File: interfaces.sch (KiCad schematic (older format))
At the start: 74 parts, among them J6 0878311420, J7 61300611121, U1 MTFC16GAPALNA-AIT, U14 XC7A100T-FGG484, U17 USB3300-EZK-TR, U18 USB3300-EZK-TR, U6 NVT2008DQ,115, Y1 TSX-3225, Y3 TSX-3225

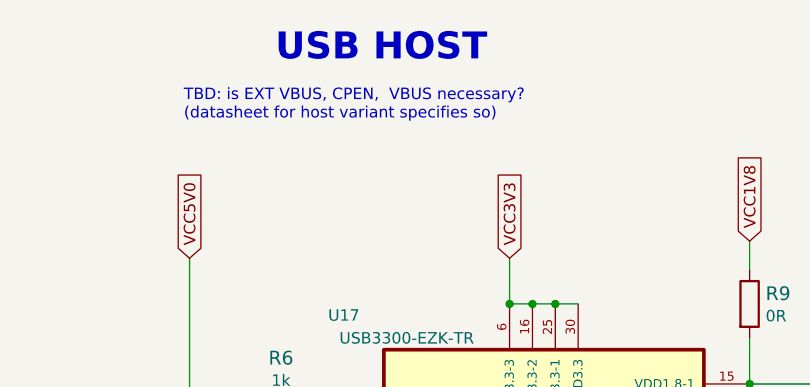
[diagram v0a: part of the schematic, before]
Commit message: Update schematic notes, update SPI0 connection
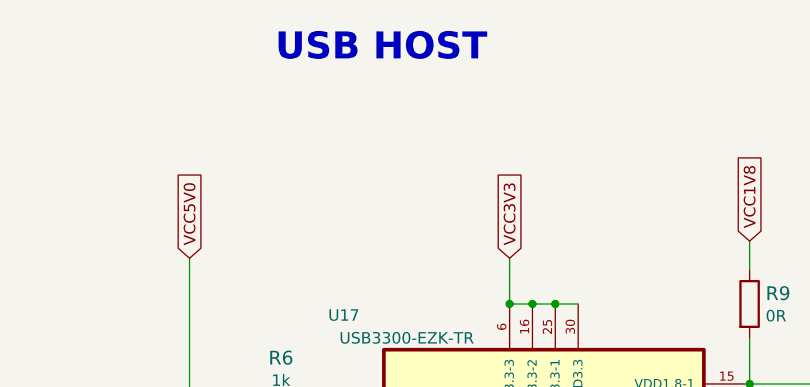
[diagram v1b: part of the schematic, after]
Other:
- note removed: "TBD: is EXT VBUS, CPEN, VBUS necessary?\n(datasheet for host variant specifies so)"
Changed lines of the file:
@@
 NoConn ~ 11400 6900
 NoConn ~ 11300 3400
-Text Notes 10625 1150 0    50   ~ 0
-TBD: is EXT VBUS, CPEN,  VBUS necessary?\n(datasheet for host variant specifies so)
 $Comp
 L artix-dc-scm:R_1M5_0402 R4

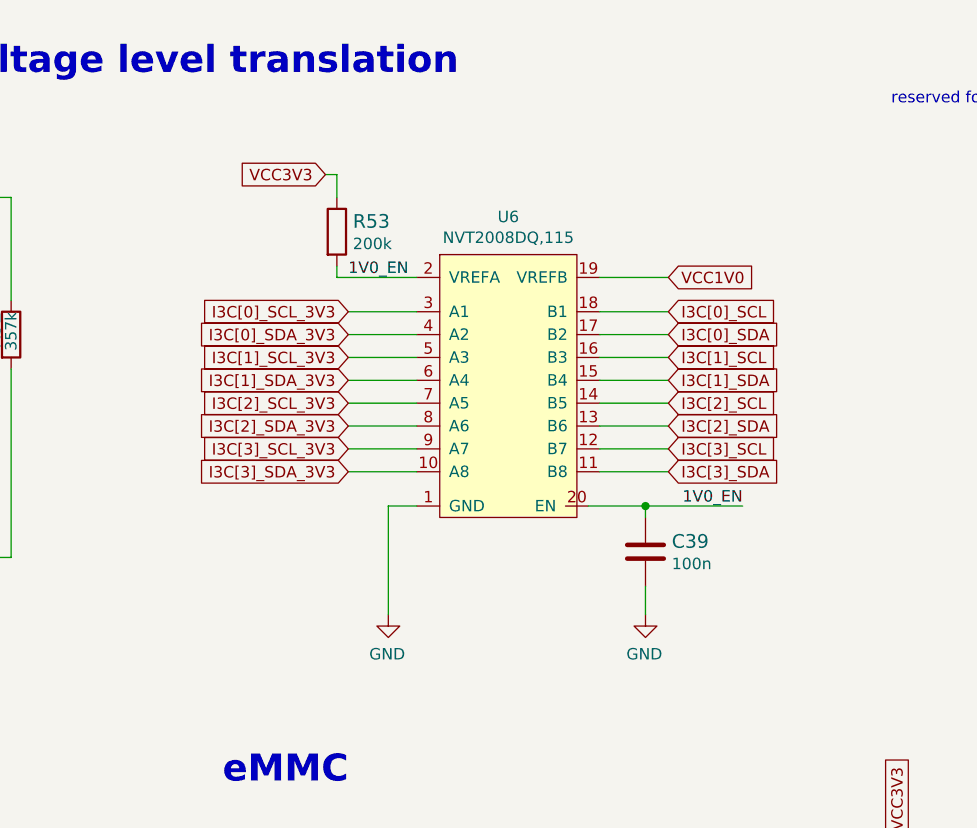
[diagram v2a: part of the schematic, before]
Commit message: Fix 1v0 translator
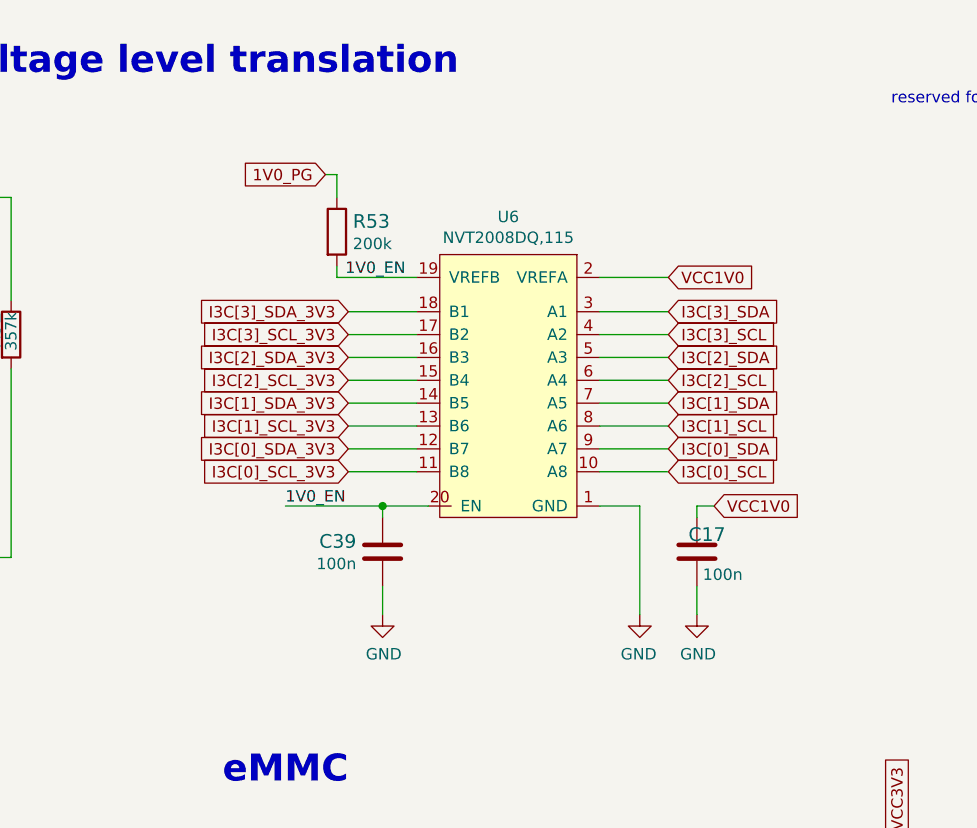
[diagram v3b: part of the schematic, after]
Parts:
- added C17: C_100n_0402, artix-dc-scm-footprints:0402-cap, symbol artix-dc-scm:C_100n_0402-artix-dc-scm
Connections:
- net 1V0_EN: now also U6.19 (VREFB); no longer U6.2 (VREFA)
- net GND: now also C17.1
- net I3C[0]_SCL: now also U6.10 (A8); no longer U6.18 (B1)
- net I3C[0]_SCL_3V3: now also U6.11 (B8); no longer U6.3 (A1)
- net I3C[0]_SDA: now also U6.9 (A7); no longer U6.17 (B2)
- net I3C[0]_SDA_3V3: now also U6.12 (B7); no longer U6.4 (A2)
- net I3C[1]_SCL: now also U6.8 (A6); no longer U6.16 (B3)
- net I3C[1]_SCL_3V3: now also U6.13 (B6); no longer U6.5 (A3)
- net I3C[1]_SDA: now also U6.7 (A5); no longer U6.15 (B4)
- net I3C[1]_SDA_3V3: now also U6.14 (B5); no longer U6.6 (A4)
- net I3C[2]_SCL: now also U6.6 (A4); no longer U6.14 (B5)
- net I3C[2]_SCL_3V3: now also U6.15 (B4); no longer U6.7 (A5)
- net I3C[2]_SDA: now also U6.5 (A3); no longer U6.13 (B6)
- net I3C[2]_SDA_3V3: now also U6.16 (B3); no longer U6.8 (A6)
- net I3C[3]_SCL: now also U6.4 (A2); no longer U6.12 (B7)
- net I3C[3]_SCL_3V3: now also U6.17 (B2); no longer U6.9 (A7)
- net I3C[3]_SDA: now also U6.3 (A1); no longer U6.11 (B8)
- net I3C[3]_SDA_3V3: now also U6.18 (B1); no longer U6.10 (A8)
- net VCC1V0: now also U6.2 (VREFA), C17.2; no longer U6.19 (VREFB)
- net VCC3V3: no longer R53.1
- new net 1V0_PG: R53.1
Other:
- moved on the sheet: C39
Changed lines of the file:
@@
 JTAG
-$Comp
-L artix-dc-scm:NVT2008DQ,115-artix-dc-scm U6
-U 1 1 628E0C73
-P 5000 6025
-F 0 "U6" H 5000 6540 50  0000 C CNN
-F 1 "NVT2008DQ,115" H 5000 6449 50  0000 C CNN
-F 2 "artix-dc-scm-footprints:QFN50P250X450X100-21N" H 5700 6775 50  0001 C CNN
-F 3 "" H 5650 6775 50  0001 C CNN
-F 4 "NVT2008BQ,115" H 5300 6875 50  0001 C CNN "MPN"
-F 5 "NXP Semiconductors" H 5400 6975 50  0001 C CNN "Manufacturer"
-	1    5000 6025
-	1    0    0    -1
-$EndComp
-Text GLabel 4300 6025 0    50   Input ~ 0
-I3C[0]_SDA_3V3
-Text GLabel 4300 6225 0    50   Input ~ 0
-I3C[1]_SDA_3V3
-Text GLabel 4300 6125 0    50   Input ~ 0
-I3C[1]_SCL_3V3
-Text GLabel 4300 6425 0    50   Input ~ 0
-I3C[2]_SDA_3V3
-Text GLabel 4300 6325 0    50   Input ~ 0
-I3C[2]_SCL_3V3
-Text GLabel 4300 6625 0    50   Input ~ 0
-I3C[3]_SDA_3V3
-Text GLabel 4300 6525 0    50   Input ~ 0
-I3C[3]_SCL_3V3
-Text GLabel 4300 5925 0    50   Input ~ 0
-I3C[0]_SCL_3V3
-Text GLabel 5700 5775 2    50   Input ~ 0
-VCC1V0
-$Comp
-L artix-dc-scm:GND-artix-dc-scm #PWR032
-U 1 1 628E4783
-P 4475 7250
-F 0 "#PWR032" H 4475 7000 50  0001 C CNN
-F 1 "GND" H 4480 7077 50  0000 C CNN
-F 2 "" H 4475 7250 50  0001 C CNN
-F 3 "" H 4475 7250 50  0001 C CNN
-	1    4475 7250
-	-1   0    0    -1
-$EndComp
-Wire Wire Line
-	4600 6775 4475 6775
-Wire Wire Line
-	4475 6775 4475 7250
-Wire Wire Line
-	4600 5925 4300 5925
-Wire Wire Line
-	4600 6025 4300 6025
-Wire Wire Line
-	4600 6125 4300 6125
-Wire Wire Line
-	4600 6225 4300 6225
-Wire Wire Line
-	4600 6325 4300 6325
-Wire Wire Line
-	4600 6425 4300 6425
-Wire Wire Line
-	4600 6525 4300 6525
-Wire Wire Line
-	4600 6625 4300 6625
-Wire Wire Line
-	5400 5925 5700 5925
-Wire Wire Line
-	5400 6025 5700 6025
-Wire Wire Line
-	5400 6125 5700 6125
-Wire Wire Line
-	5400 6225 5700 6225
-Wire Wire Line
-	5400 6325 5700 6325
-Wire Wire Line
-	5400 6425 5700 6425
-Wire Wire Line
-	5400 6525 5700 6525
-Wire Wire Line
-	5400 6625 5700 6625
-Text GLabel 4200 5325 0    50   Input ~ 0
-VCC3V3
-Wire Wire Line
-	4600 5775 4250 5775
-Wire Wire Line
-	5700 5775 5400 5775
-Wire Wire Line
-	6025 6775 5600 6775
-Text Label 6025 6775 2    50   ~ 0
-1V0_EN
 $Comp
 L artix-dc-scm:R_357k_0402-artix-dc-scm R46
@@
 Wire Wire Line
 	2725 5425 2825 5425
-$Comp
-L artix-dc-scm:R_200k_0402-artix-dc-scm R53
-U 1 1 61B2DA1A
-P 4250 5575
-F 0 "R53" V 4205 5645 60  0000 L CNN
-F 1 "R_200k_0402" H 4250 5425 60  0001 C CNN
-F 2 "artix-dc-scm-footprints:0402-res" H 4450 5775 60  0001 L CNN
-F 3 "" H 4250 5575 50  0001 C CNN
-F 4 "YAGEO_(PHYCOMP)" H 4450 5975 60  0001 L CNN "Manufacturer"
-F 5 "RC0402FR-07200KL" H 4450 5875 60  0001 L CNN "MPN"
-F 6 "200k" V 4303 5645 50  0000 L CNN "Val"
-	1    4250 5575
-	0    1    1    0
-$EndComp
-Wire Wire Line
-	4250 5775 4250 5725
-Wire Wire Line
-	4250 5425 4250 5325
-Wire Wire Line
-	4200 5325 4250 5325
-Text Label 4300 5775 0    50   ~ 0
-1V0_EN
-$Comp
-L artix-dc-scm:C_100n_0402-artix-dc-scm C39
-U 1 1 61B2DA1B
-P 5600 6975
-F 0 "C39" H 5485 6930 60  0000 R CNN
-F 1 "C_100n_0402" H 5600 6825 60  0001 C CNN
-F 2 "artix-dc-scm-footprints:0402-cap" H 5800 7175 60  0001 L CNN
-F 3 "" H 5600 6975 50  0001 C CNN
-F 4 "Walsin" H 5800 7375 60  0001 L CNN "Manufacturer"
-F 5 "0402X104K6R3CT" H 5800 7275 60  0001 L CNN "MPN"
-F 6 "100n" H 5485 7028 50  0000 R CNN "Val"
-	1    5600 6975
-	-1   0    0    1
-$EndComp
-Wire Wire Line
-	5600 6775 5600 6825
-Connection ~ 5600 6775
-Wire Wire Line
-	5600 6775 5350 6775
-$Comp
-L artix-dc-scm:GND-artix-dc-scm #PWR034
-U 1 1 61B2DA1C
-P 5600 7250
-F 0 "#PWR034" H 5600 7000 50  0001 C CNN
-F 1 "GND" H 5605 7077 50  0000 C CNN
-F 2 "" H 5600 7250 50  0001 C CNN
-F 3 "" H 5600 7250 50  0001 C CNN
-	1    5600 7250
-	-1   0    0    -1
-$EndComp
-Wire Wire Line
-	5600 7125 5600 7250
 Text Notes 2200 4900 0    118  ~ 24
 I3C voltage level translation
@@
 Wire Wire Line
 	2125 2850 2125 2725
-Text GLabel 5700 5925 2    50   Input ~ 0
-I3C[0]_SCL
-Text GLabel 5700 6025 2    50   Input ~ 0
-I3C[0]_SDA
-Text GLabel 5700 6125 2    50   Input ~ 0
-I3C[1]_SCL
-Text GLabel 5700 6225 2    50   Input ~ 0
-I3C[1]_SDA
-Text GLabel 5700 6325 2    50   Input ~ 0
-I3C[2]_SCL
-Text GLabel 5700 6425 2    50   Input ~ 0
-I3C[2]_SDA
-Text GLabel 5700 6525 2    50   Input ~ 0
-I3C[3]_SCL
-Text GLabel 5700 6625 2    50   Input ~ 0
-I3C[3]_SDA
 $Comp
 L artix-dc-scm:C_100n_0402-artix-dc-scm C189
@@
 Text Notes 4650 1350 0    50   ~ 0
 TODO: The PCIe x1 connection must be confirmed by synthesis
+$Comp
+L artix-dc-scm:NVT2008DQ,115-artix-dc-scm U6
+U 1 1 628E0C73
+P 5000 6025
+F 0 "U6" H 5000 6540 50  0000 C CNN
+F 1 "NVT2008DQ,115" H 5000 6449 50  0000 C CNN
+F 2 "artix-dc-scm-footprints:QFN50P250X450X100-21N" H 5700 6775 50  0001 C CNN
+F 3 "" H 5650 6775 50  0001 C CNN
+F 4 "NVT2008BQ,115" H 5300 6875 50  0001 C CNN "MPN"
+F 5 "NXP Semiconductors" H 5400 6975 50  0001 C CNN "Manufacturer"
+	1    5000 6025
+	-1   0    0    -1
+$EndComp
+Wire Wire Line
+	4450 7125 4450 7250
+$Comp
+L artix-dc-scm:GND-artix-dc-scm #PWR034
+U 1 1 61B2DA1C
+P 4450 7250
+F 0 "#PWR034" H 4450 7000 50  0001 C CNN
+F 1 "GND" H 4455 7077 50  0000 C CNN
+F 2 "" H 4450 7250 50  0001 C CNN
+F 3 "" H 4450 7250 50  0001 C CNN
+	1    4450 7250
+	1    0    0    -1
+$EndComp
+Wire Wire Line
+	4450 6775 4650 6775
+Connection ~ 4450 6775
+Wire Wire Line
+	4450 6775 4450 6825
+$Comp
+L artix-dc-scm:C_100n_0402-artix-dc-scm C39
+U 1 1 61B2DA1B
+P 4450 6975
+F 0 "C39" H 4335 6930 60  0000 R CNN
+F 1 "C_100n_0402" H 4450 6825 60  0001 C CNN
+F 2 "artix-dc-scm-footprints:0402-cap" H 4650 7175 60  0001 L CNN
+F 3 "" H 4450 6975 50  0001 C CNN
+F 4 "Walsin" H 4650 7375 60  0001 L CNN "Manufacturer"
+F 5 "0402X104K6R3CT" H 4650 7275 60  0001 L CNN "MPN"
+F 6 "100n" H 4335 7028 50  0000 R CNN "Val"
+	1    4450 6975
+	1    0    0    1
+$EndComp
+Text Label 4025 6775 0    50   ~ 0
+1V0_EN
+Wire Wire Line
+	4025 6775 4450 6775
+Wire Wire Line
+	5700 5775 5400 5775
+Wire Wire Line
+	5400 5925 5700 5925
+Wire Wire Line
+	5400 6025 5700 6025
+Wire Wire Line
+	5400 6125 5700 6125
+Wire Wire Line
+	5400 6225 5700 6225
+Wire Wire Line
+	5400 6325 5700 6325
+Wire Wire Line
+	5400 6425 5700 6425
+Wire Wire Line
+	5400 6525 5700 6525
+Wire Wire Line
+	5400 6625 5700 6625
+Text GLabel 5700 5775 2    50   Input ~ 0
+VCC1V0
+Wire Wire Line
+	4250 5775 4250 5725
+$Comp
+L artix-dc-scm:R_200k_0402-artix-dc-scm R53
+U 1 1 61B2DA1A
+P 4250 5575
+F 0 "R53" V 4205 5645 60  0000 L CNN
+F 1 "R_200k_0402" H 4250 5425 60  0001 C CNN
+F 2 "artix-dc-scm-footprints:0402-res" H 4450 5775 60  0001 L CNN
+F 3 "" H 4250 5575 50  0001 C CNN
+F 4 "YAGEO_(PHYCOMP)" H 4450 5975 60  0001 L CNN "Manufacturer"
+F 5 "RC0402FR-07200KL" H 4450 5875 60  0001 L CNN "MPN"
+F 6 "200k" V 4303 5645 50  0000 L CNN "Val"
+	1    4250 5575
+	0    1    1    0
+$EndComp
+Wire Wire Line
+	4600 5775 4250 5775
+Wire Wire Line
+	4600 5925 4300 5925
+Wire Wire Line
+	4600 6025 4300 6025
+Wire Wire Line
+	4600 6125 4300 6125
+Wire Wire Line
+	4600 6225 4300 6225
+Wire Wire Line
+	4600 6325 4300 6325
+Wire Wire Line
+	4600 6425 4300 6425
+Wire Wire Line
+	4600 6525 4300 6525
+Wire Wire Line
+	4600 6625 4300 6625
+Wire Wire Line
+	5575 6775 5575 7250
+Wire Wire Line
+	5400 6775 5575 6775
+$Comp
+L artix-dc-scm:GND-artix-dc-scm #PWR032
+U 1 1 628E4783
+P 5575 7250
+F 0 "#PWR032" H 5575 7000 50  0001 C CNN
+F 1 "GND" H 5580 7077 50  0000 C CNN
+F 2 "" H 5575 7250 50  0001 C CNN
+F 3 "" H 5575 7250 50  0001 C CNN
+	1    5575 7250
+	-1   0    0    -1
+$EndComp
+Text GLabel 4300 6625 0    50   Input ~ 0
+I3C[0]_SCL_3V3
+Text GLabel 4300 6025 0    50   Input ~ 0
+I3C[3]_SCL_3V3
+Text GLabel 4300 5925 0    50   Input ~ 0
+I3C[3]_SDA_3V3
+Text GLabel 4300 6225 0    50   Input ~ 0
+I3C[2]_SCL_3V3
+Text GLabel 4300 6125 0    50   Input ~ 0
+I3C[2]_SDA_3V3
+Text GLabel 4300 6425 0    50   Input ~ 0
+I3C[1]_SCL_3V3
+Text GLabel 4300 6325 0    50   Input ~ 0
+I3C[1]_SDA_3V3
+Text GLabel 4300 6525 0    50   Input ~ 0
+I3C[0]_SDA_3V3
+Text GLabel 4200 5325 0    50   Input ~ 0
+1V0_PG
+Text Label 4550 5775 2    50   ~ 0
+1V0_EN
+Text GLabel 5700 6625 2    50   Input ~ 0
+I3C[0]_SCL
+Text GLabel 5700 6525 2    50   Input ~ 0
+I3C[0]_SDA
+Text GLabel 5700 6425 2    50   Input ~ 0
+I3C[1]_SCL
+Text GLabel 5700 6325 2    50   Input ~ 0
+I3C[1]_SDA
+Text GLabel 5700 6225 2    50   Input ~ 0
+I3C[2]_SCL
+Text GLabel 5700 6125 2    50   Input ~ 0
+I3C[2]_SDA
+Text GLabel 5700 6025 2    50   Input ~ 0
+I3C[3]_SCL
+Text GLabel 5700 5925 2    50   Input ~ 0
+I3C[3]_SDA
+Wire Wire Line
+	5825 7125 5825 7250
+$Comp
+L artix-dc-scm:GND-artix-dc-scm #PWR0128
+U 1 1 60C1CFA2
+P 5825 7250
+F 0 "#PWR0128" H 5825 7000 50  0001 C CNN
+F 1 "GND" H 5830 7077 50  0000 C CNN
+F 2 "" H 5825 7250 50  0001 C CNN
+F 3 "" H 5825 7250 50  0001 C CNN
+	1    5825 7250
+	1    0    0    -1
+$EndComp
+$Comp
+L artix-dc-scm:C_100n_0402-artix-dc-scm C17
+U 1 1 60C1CFAB
+P 5825 6975
+F 0 "C17" H 5950 6900 60  0000 R CNN
+F 1 "C_100n_0402" H 5825 6825 60  0001 C CNN
+F 2 "artix-dc-scm-footprints:0402-cap" H 6025 7175 60  0001 L CNN
+F 3 "" H 5825 6975 50  0001 C CNN
+F 4 "Walsin" H 6025 7375 60  0001 L CNN "Manufacturer"
+F 5 "0402X104K6R3CT" H 6025 7275 60  0001 L CNN "MPN"
+F 6 "100n" H 6025 7075 50  0000 R CNN "Val"
+	1    5825 6975
+	1    0    0    1
+$EndComp
+Wire Wire Line
+	4250 5425 4250 5325
+Wire Wire Line
+	4200 5325 4250 5325
+Wire Wire Line
+	5900 6775 5825 6775
+Wire Wire Line
+	5825 6825 5825 6775
+Text GLabel 5900 6775 2    50   Input ~ 0
+VCC1V0
 $EndSCHEMATC

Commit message: Add JTAG FTDI to schematic
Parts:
- added C? (x9): C_100n_0402, artix-dc-scm-footprints:0402-cap, symbol artix-dc-scm:C_100n_0402
- added C? (x2): C_4u7_0402, artix-dc-scm-footprints:0402-cap, symbol artix-dc-scm:C_4u7_0402
- added C?: C_3u3_0603, artix-dc-scm-footprints:0603-cap, symbol artix-dc-scm:C_3u3_0603
- added FB? (x2): BLM15AG601SN1D, artix-dc-scm-footprints:0402-res, symbol artix-dc-scm:BLM15AG601SN1D
- added J?: 10118192-0001LF, artix-dc-scm-footprints:USB_Micro_B_Female_10118192, symbol artix-dc-scm:10118192-0001LF
- added R?: R_12k_0402, artix-dc-scm-footprints:0402-res, symbol artix-dc-scm:R_12k_0402
- added R? (x2): R_10k_0402, artix-dc-scm-footprints:0402-res, symbol artix-dc-scm:R_10k_0402
- added R? (x2): R_4k7_0402, artix-dc-scm-footprints:0402-res, symbol artix-dc-scm:R_4k7_0402
- added R?: R_1k_0402, artix-dc-scm-footprints:0402-res, symbol artix-dc-scm:R_1k_0402
- added TP? (x3): TP_SMD1MM, artix-dc-scm-footprints:Testpoint_smd_1mm, symbol artix-dc-scm:TP_SMD1MM
- added U?: FT2232H-56Q, artix-dc-scm-footprints:QFN-56-1EP_8x8mm_P0.5mm_EP5.5.9x5.9mm, symbol artix-dc-scm:FT2232H-56Q
- added Y?: ASFLMB-12.000MHZ-LC-T, artix-dc-scm-footprints:ASFLMB, symbol artix-dc-scm:ASFLMB-12.000MHZ-LC-T
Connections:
- net GND: now also U1.H2 (VSSQ), U1.H9 (VSSQ), U1.L3 (VSSQ), U1.L8 (VSSQ), U1.M4 (VSSQ), U1.M7 (VSSQ), U1.P2 (VSSQ), U1.P9 (VSSQ), C?.2, C?.2, C?.2, C?.2, C?.2, C?.2, C?.2, C?.2, C?.2, C?.2, C?.2, C?.2, J?.5, J?.SH, R?.2, R?.2, R?.2, U?.10 (TEST), U?.21 (GND), U?.41 (GND), U?.45 (GND), Y?.2 (GND)
- net JTAG_TCK: now also U?.12 (ADBUS0)
- net JTAG_TDI: now also U?.13 (ADBUS1)
- net JTAG_TDO: now also U?.14 (ADBUS2)
- net JTAG_TMS: now also U?.15 (ADBUS3)
- net VCC3V3: now also C?.1, C?.1, C?.1, C?.1, C?.1, FB?.1, FB?.1, R?.1, U?.16 (VCCIO), U?.36 (VCCIO), U?.44 (VREGIN), U?.50 (VCCIO), Y?.1 (#STB), Y?.4 (VDD)
- new net: R?.1, R?.2, R?.2, U?.11 (RESET)
- new net: C?.1, C?.1, C?.1, U?.2 (VCORE), U?.31 (VCORE), U?.43 (VREGOUT)
- new net: U?.3 (OSCI), Y?.3 (OUT)
- new net: TP?.1, U?.30 (SUSPEND)
- new net: C?.1, C?.1, FB?.2, U?.5 (VPHY)
- new net: R?.1, R?.2, U?.53 (BCBUS7)
- new net: TP?.1, U?.54 (PWREN)
- new net: R?.1, U?.6 (REF)
- new net: C?.1, C?.1, FB?.2, U?.9 (VPLL)
- new net: J?.4, TP?.1
- new net DBG_USB_D_N: J?.2, U?.7 (DM)
- new net DBG_USB_D_P: J?.3, U?.8 (DP)
- new net VBUS: J?.1, R?.1, R?.1
- no-connect marks 9 -> 13
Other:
- note added: "Debug USB"
- note added: "FTDI"
- note removed: "TODO: The PCIe x1 connection must be confirmed by synthesis"
- moved on the sheet: C10, C11, C12, C13, C17, C18, C183, C184, C185, C186, C187, C188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
